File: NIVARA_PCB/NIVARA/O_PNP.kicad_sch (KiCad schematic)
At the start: 4 parts, among them Q6 NCV8402xST

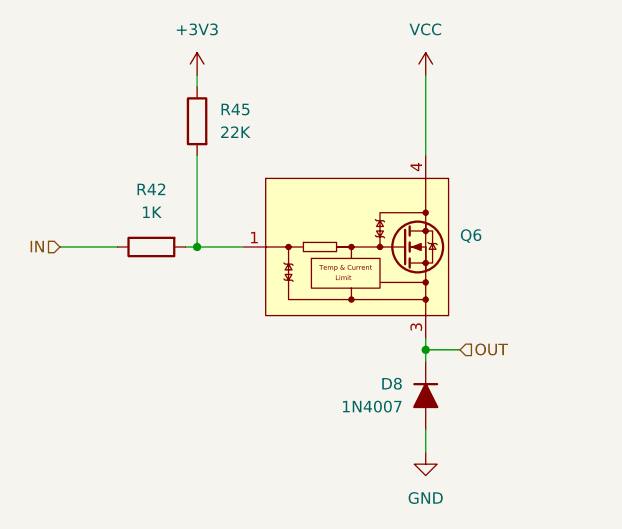
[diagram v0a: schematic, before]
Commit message: arreglo del desastre que tenia con las salidas PNP
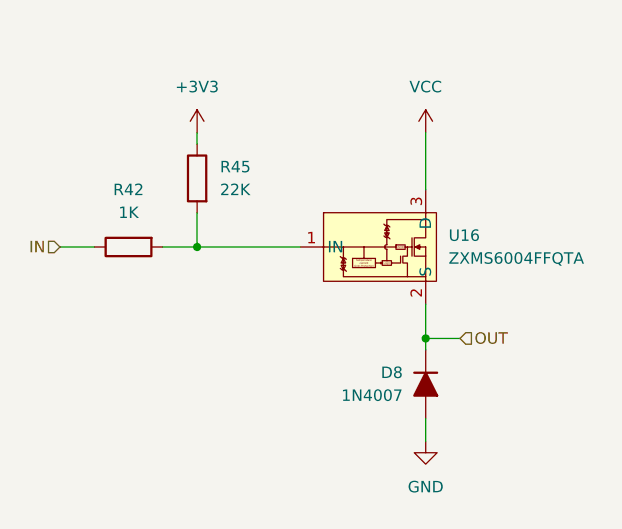
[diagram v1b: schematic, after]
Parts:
- removed Q6: NCV8402xST, Package_TO_SOT_SMD:SOT-223, symbol Driver_FET:NCV8402xST
- added U16: ZXMS6004FFQTA, easyeda2kicad:SOT-23F_L2.9-W1.8-P0.95-LS2.4-BR, symbol CUSTOM:ZXMS6004FFQTA
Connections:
- net OUT: now also U16.2 (S)
- net VCC: now also U16.3 (D)
- net at R42.1, R45.1: now also U16.1 (IN)
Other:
- moved on the sheet: D8, R42, R45
